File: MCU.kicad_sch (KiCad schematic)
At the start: 56 parts, among them J4 SWD, J5 SSD1306, Q13 AO3404A, SW1 EC11E15244G1, U12 FT234XD, U2 STM32G474CEUx, Y1 8M

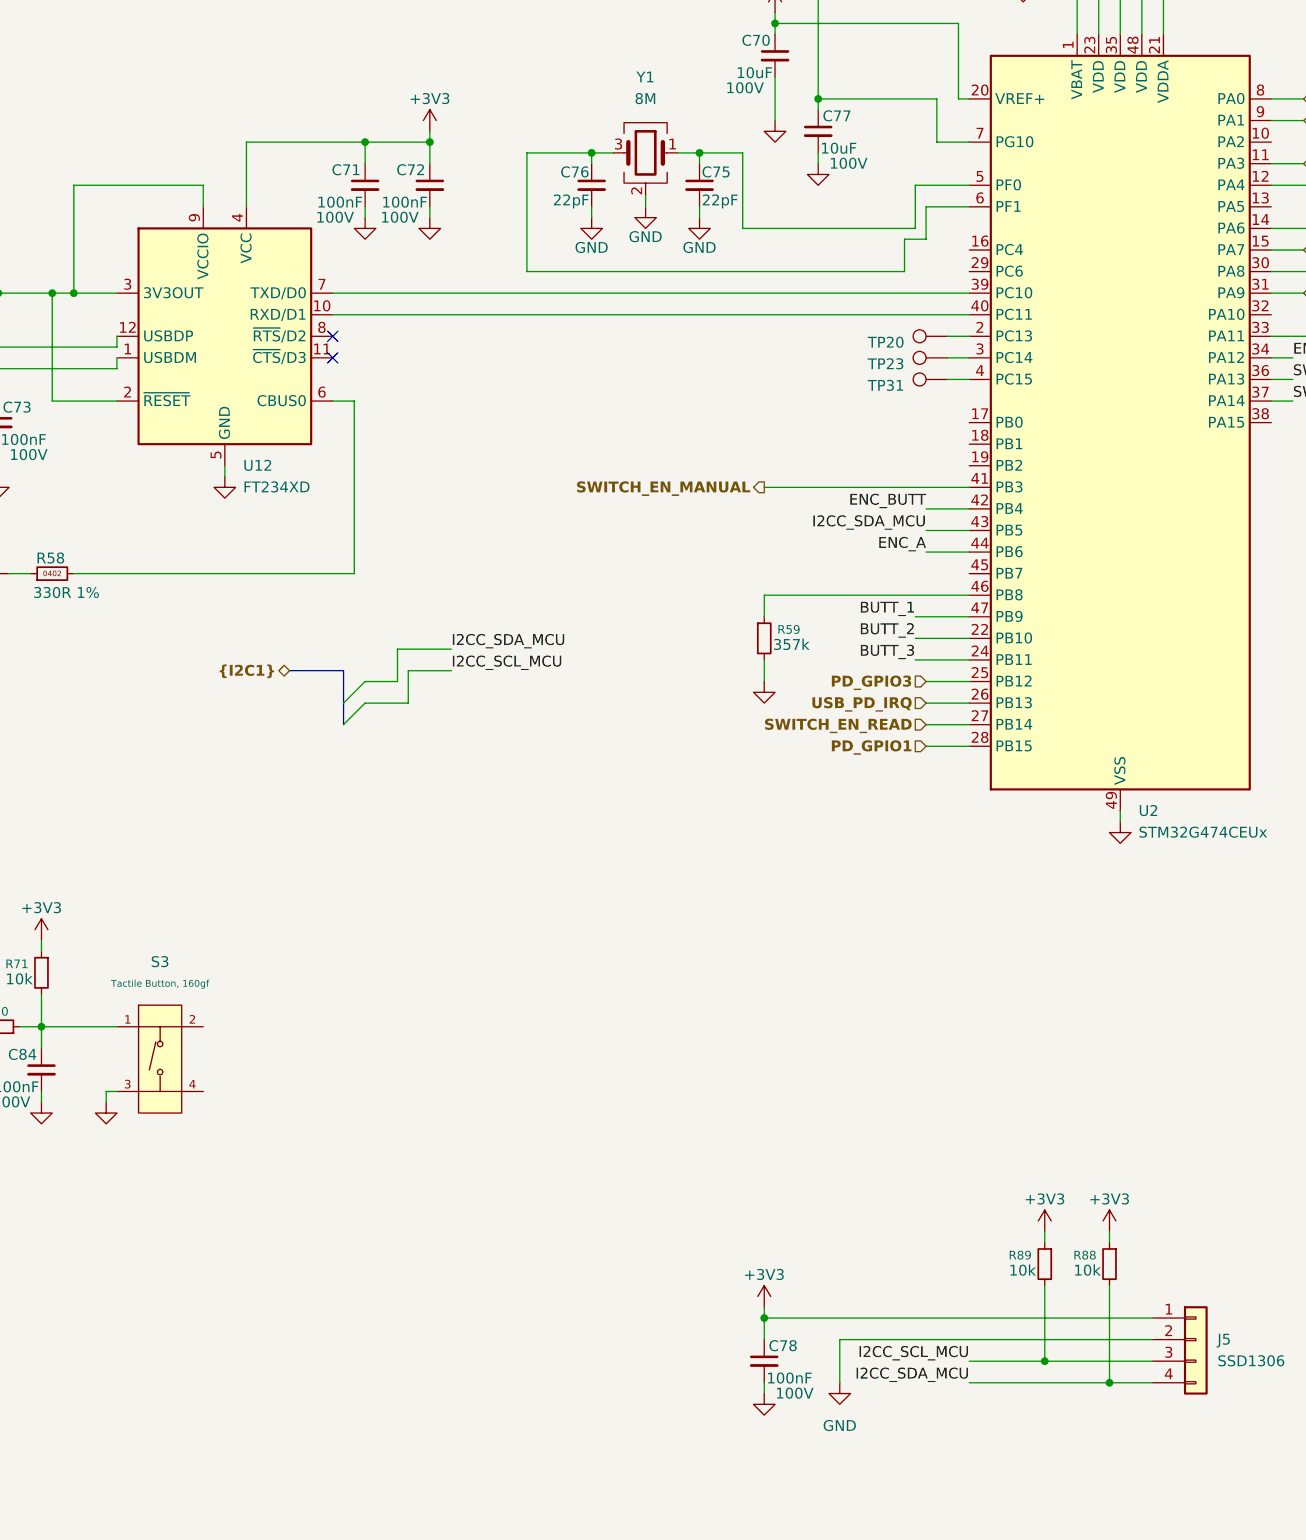
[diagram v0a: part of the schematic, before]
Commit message: changed mistakes on board, first firmware version
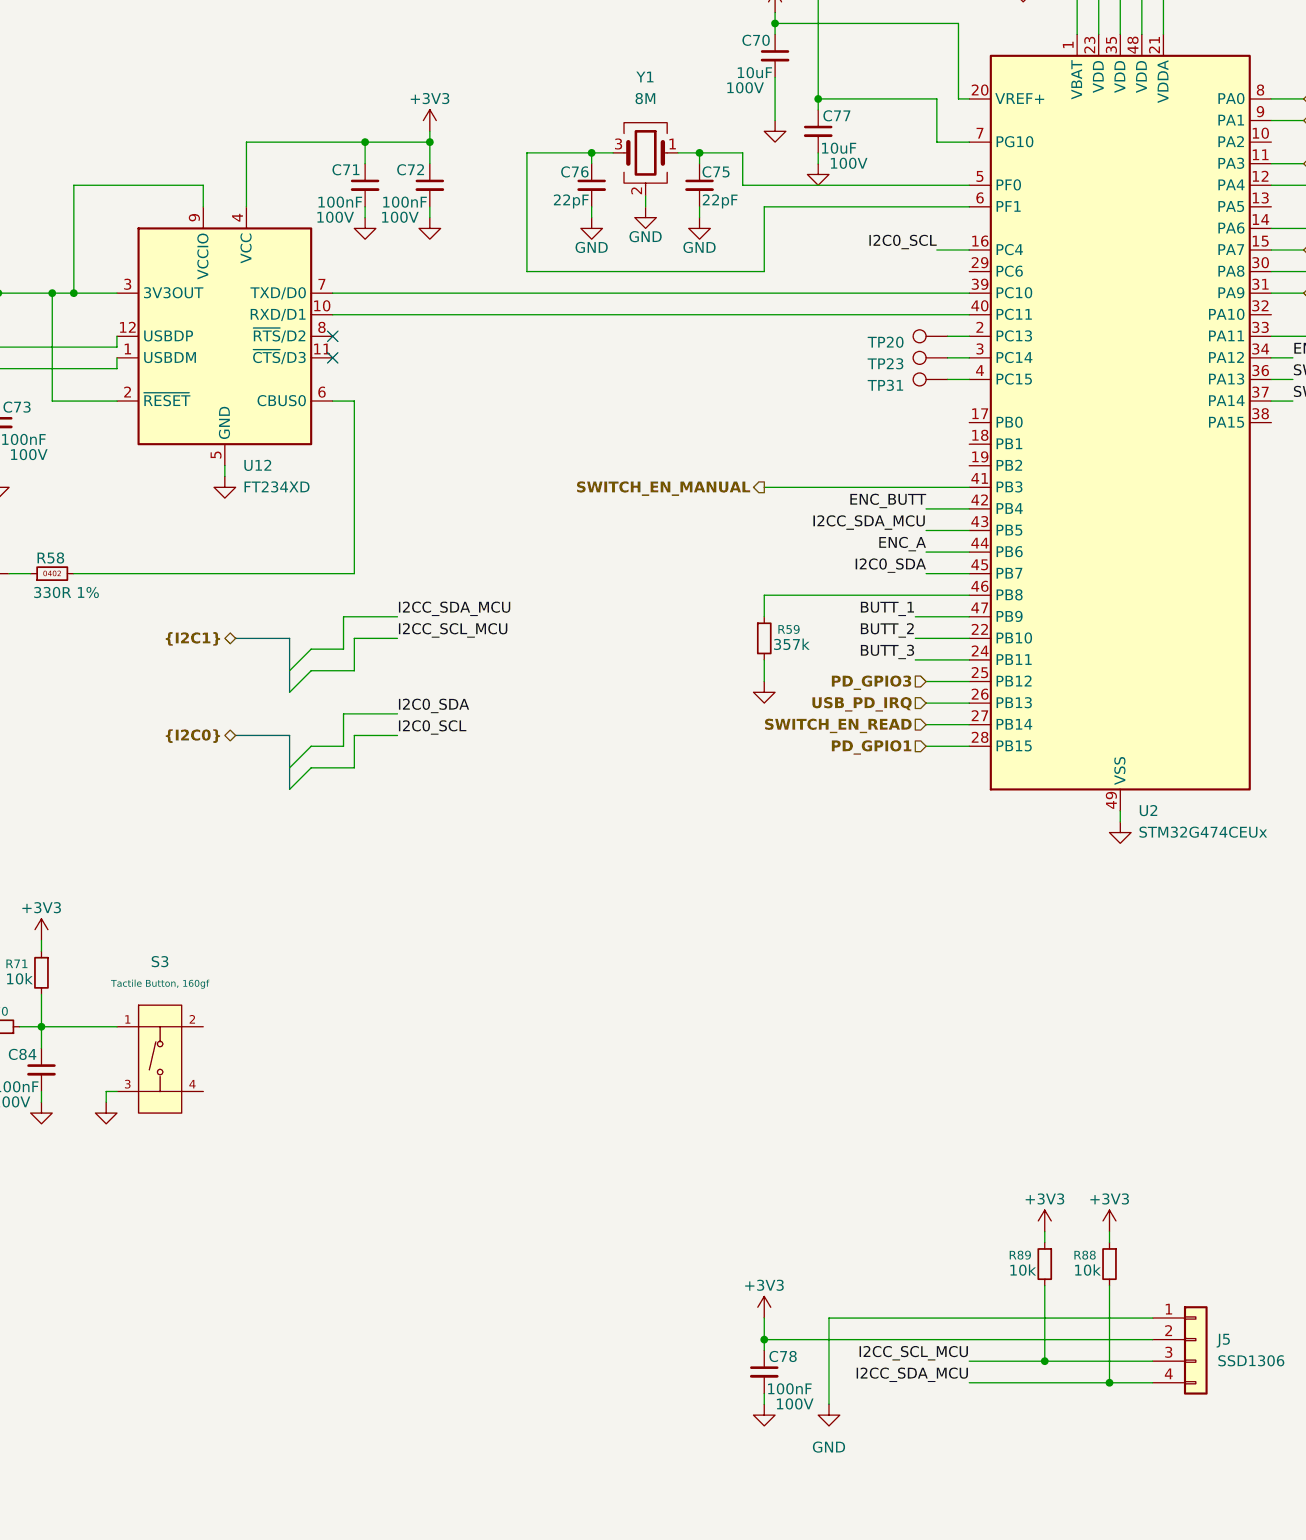
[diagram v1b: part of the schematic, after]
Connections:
- net +3V3: now also J5.2 (Pin_2); no longer J5.1 (Pin_1)
- net GND: now also J5.1 (Pin_1); no longer J5.2 (Pin_2)
- net I2C0_SCL: now reaches U2.16 (PC4)
- net I2C0_SDA: now reaches U2.45 (PB7)
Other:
- moved on the sheet: C78

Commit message: first working firmware
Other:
- note added: "Reset button please and tagconnect reset"
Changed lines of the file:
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@@
 		(rev "R1")
+	)
+	(text "Reset button please\nand tagconnect reset"
+		(exclude_from_sim no)
+		(at 194.056 93.98 0)
+		(effects
+			(font
+				(size 1.27 1.27)
+			)
+		)
 	)
 	(junction

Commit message: Changed UI around a bit, and improved CV handling
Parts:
- added R33: 10k, Resistor_SMD:R_0402_1005Metric, symbol Device:R_Small
- C77: value 10uF -> 100nF; footprint Capacitor_SMD:C_1210_3225Metric -> Capacitor_SMD:C_0402_1005Metric; LCSC C5156756 -> C162178
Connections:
- net +3V3: now also R33.1; no longer C77.1, U2.7 (PG10)
- net at U12.10 (RXD/D1): now also U2.39 (PC10); no longer U2.40 (PC11)
- net at U12.7 (TXD/D0): now also U2.40 (PC11); no longer U2.39 (PC10)
- new net: C77.1, R33.2, U2.7 (PG10)
